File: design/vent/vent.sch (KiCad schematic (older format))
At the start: 20 parts, among them J1 Conn_01x02, J10 CS_TEST, J2 Conn_01x02, J3 SDA_TEST, J4 RX_TEST, J5 TX_TEST, J6 SCL_TEST, J7 SCK_TEST, J8 MISO_TEST, J9 MOSI_TEST

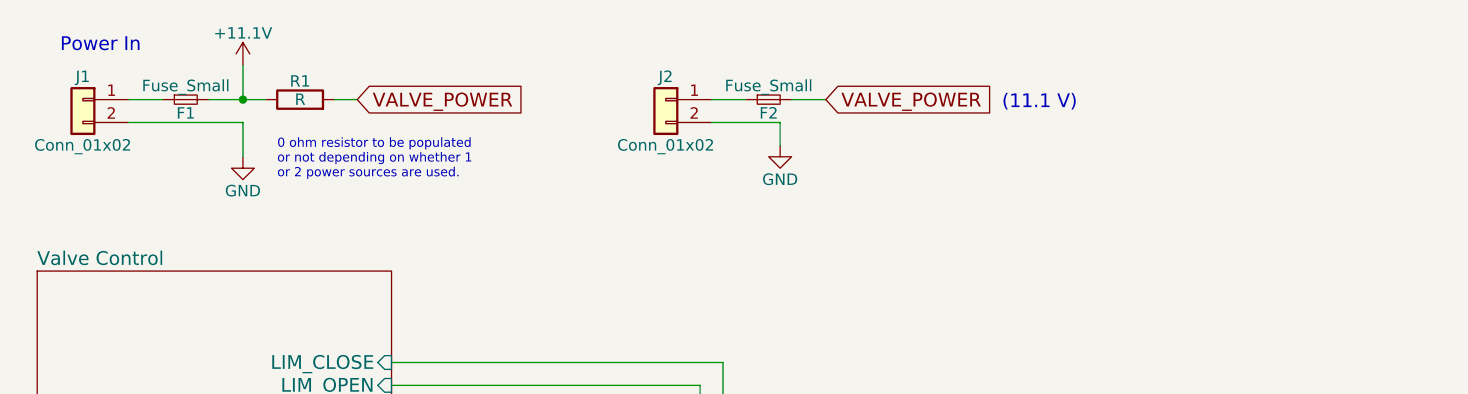
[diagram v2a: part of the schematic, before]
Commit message: Merge control power and analog sensor connectors
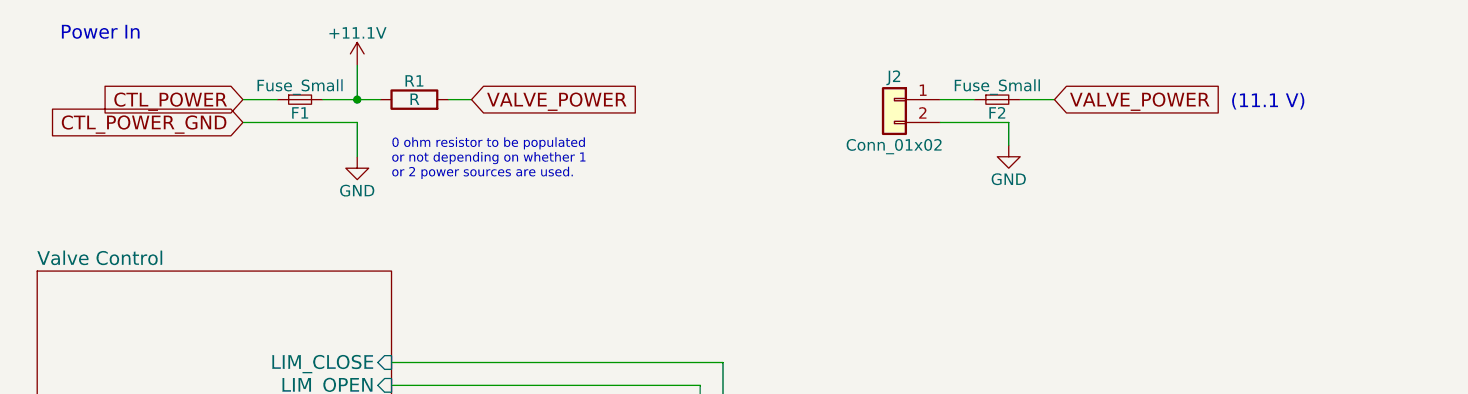
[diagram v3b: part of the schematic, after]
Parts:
- removed J1: Conn_01x02, symbol Conn_01x02
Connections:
- net CTL_POWER: now reaches F1.1
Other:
- moved on the sheet: F1, F2, J2, R1
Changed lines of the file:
@@
 NoConn ~ 6100 3650
 NoConn ~ 6100 3750
-$Comp
-L Conn_01x02 J1
-U 1 1 5ADF7D10
-P 1800 1350
-F 0 "J1" H 1800 1450 50  0000 C CNN
-F 1 "Conn_01x02" H 1800 1150 50  0000 C CNN
-F 2 "" H 1800 1350 50  0001 C CNN
-F 3 "" H 1800 1350 50  0001 C CNN
-	1    1800 1350
-	-1   0    0    -1
-$EndComp
-Text Notes 1700 1150 0    60   ~ 0
+Text Notes 1700 1100 0    60   ~ 0
 Power In
 $Comp
 L +11.1V #PWR1
 U 1 1 5ADF8011
-P 2500 1200
-F 0 "#PWR1" H 2500 1050 50  0001 C CNN
-F 1 "+11.1V" H 2500 1340 50  0000 C CNN
-F 2 "" H 2500 1200 50  0001 C CNN
-F 3 "" H 2500 1200 50  0001 C CNN
-	1    2500 1200
+P 3000 1200
+F 0 "#PWR1" H 3000 1050 50  0001 C CNN
+F 1 "+11.1V" H 3000 1340 50  0000 C CNN
+F 2 "" H 3000 1200 50  0001 C CNN
+F 3 "" H 3000 1200 50  0001 C CNN
+	1    3000 1200
 	1    0    0    -1
 $EndComp
@@
 L GND #PWR3
 U 1 1 5ADF8038
-P 2500 1600
-F 0 "#PWR3" H 2500 1350 50  0001 C CNN
-F 1 "GND" H 2500 1450 50  0000 C CNN
-F 2 "" H 2500 1600 50  0001 C CNN
-F 3 "" H 2500 1600 50  0001 C CNN
-	1    2500 1600
+P 3000 1600
+F 0 "#PWR3" H 3000 1350 50  0001 C CNN
+F 1 "GND" H 3000 1450 50  0000 C CNN
+F 2 "" H 3000 1600 50  0001 C CNN
+F 3 "" H 3000 1600 50  0001 C CNN
+	1    3000 1600
 	1    0    0    -1
 $EndComp
@@
 L Fuse_Small F1
 U 1 1 5AE9CD78
-P 2250 1350
-F 0 "F1" H 2250 1290 50  0000 C CNN
-F 1 "Fuse_Small" H 2250 1410 50  0000 C CNN
-F 2 "" H 2250 1350 50  0001 C CNN
-F 3 "" H 2250 1350 50  0001 C CNN
-	1    2250 1350
+P 2750 1350
+F 0 "F1" H 2750 1290 50  0000 C CNN
+F 1 "Fuse_Small" H 2750 1410 50  0000 C CNN
+F 2 "" H 2750 1350 50  0001 C CNN
+F 3 "" H 2750 1350 50  0001 C CNN
+	1    2750 1350
 	1    0    0    -1
 $EndComp
@@
 	4900 4950 5100 4950
 Wire Wire Line
-	2500 1200 2500 1350
-Wire Wire Line
-	2500 1450 2500 1600
-Wire Wire Line
-	2000 1450 2500 1450
+	3000 1200 3000 1350
+Wire Wire Line
+	3000 1450 3000 1600
+Wire Wire Line
+	2500 1450 3000 1450
 Wire Wire Line
 	5500 3250 5500 3050
@@
 Connection ~ 3900 5950
 Wire Wire Line
-	2000 1350 2150 1350
-Wire Wire Line
-	2350 1350 2600 1350
+	2500 1350 2650 1350
+Wire Wire Line
+	2850 1350 3100 1350
 Wire Wire Line
 	3150 2500 4600 2500
@@
 L Conn_01x02 J2
 U 1 1 5AEFA083
-P 4350 1350
-F 0 "J2" H 4350 1450 50  0000 C CNN
-F 1 "Conn_01x02" H 4350 1150 50  0000 C CNN
-F 2 "" H 4350 1350 50  0001 C CNN
-F 3 "" H 4350 1350 50  0001 C CNN
-	1    4350 1350
+P 5350 1350
+F 0 "J2" H 5350 1450 50  0000 C CNN
+F 1 "Conn_01x02" H 5350 1150 50  0000 C CNN
+F 2 "" H 5350 1350 50  0001 C CNN
+F 3 "" H 5350 1350 50  0001 C CNN
+	1    5350 1350
 	-1   0    0    -1
 $EndComp
@@
 L GND #PWR2
 U 1 1 5AEFA08B
-P 4850 1550
-F 0 "#PWR2" H 4850 1300 50  0001 C CNN
-F 1 "GND" H 4850 1400 50  0000 C CNN
-F 2 "" H 4850 1550 50  0001 C CNN
-F 3 "" H 4850 1550 50  0001 C CNN
-	1    4850 1550
+P 5850 1550
+F 0 "#PWR2" H 5850 1300 50  0001 C CNN
+F 1 "GND" H 5850 1400 50  0000 C CNN
+F 2 "" H 5850 1550 50  0001 C CNN
+F 3 "" H 5850 1550 50  0001 C CNN
+	1    5850 1550
 	-1   0    0    -1
 $EndComp
-Text Notes 6150 1400 2    60   ~ 0
+Text Notes 7150 1400 2    60   ~ 0
 (11.1 V)
 $Comp
 L Fuse_Small F2
 U 1 1 5AEFA092
-P 4800 1350
-F 0 "F2" H 4800 1290 50  0000 C CNN
-F 1 "Fuse_Small" H 4800 1410 50  0000 C CNN
-F 2 "" H 4800 1350 50  0001 C CNN
-F 3 "" H 4800 1350 50  0001 C CNN
-	1    4800 1350
-	1    0    0    -1
-$EndComp
-Wire Wire Line
-	4700 1350 4550 1350
-Wire Wire Line
-	4850 1550 4850 1450
-Wire Wire Line
-	4850 1450 4550 1450
-Wire Wire Line
-	5050 1350 4900 1350
-Text GLabel 5050 1350 2    60   Input ~ 0
+P 5800 1350
+F 0 "F2" H 5800 1290 50  0000 C CNN
+F 1 "Fuse_Small" H 5800 1410 50  0000 C CNN
+F 2 "" H 5800 1350 50  0001 C CNN
+F 3 "" H 5800 1350 50  0001 C CNN
+	1    5800 1350
+	1    0    0    -1
+$EndComp
+Wire Wire Line
+	5700 1350 5550 1350
+Wire Wire Line
+	5850 1550 5850 1450
+Wire Wire Line
+	5850 1450 5550 1450
+Wire Wire Line
+	6050 1350 5900 1350
+Text GLabel 6050 1350 2    60   Input ~ 0
 VALVE_POWER
-Text GLabel 3000 1350 2    60   Input ~ 0
+Text GLabel 3500 1350 2    60   Input ~ 0
 VALVE_POWER
 $Comp
 L R R1
 U 1 1 5AEFB0AE
-P 2750 1350
-F 0 "R1" V 2830 1350 50  0000 C CNN
-F 1 "R" V 2750 1350 50  0000 C CNN
-F 2 "" V 2680 1350 50  0001 C CNN
-F 3 "" H 2750 1350 50  0001 C CNN
-	1    2750 1350
+P 3250 1350
+F 0 "R1" V 3330 1350 50  0000 C CNN
+F 1 "R" V 3250 1350 50  0000 C CNN
+F 2 "" V 3180 1350 50  0001 C CNN
+F 3 "" H 3250 1350 50  0001 C CNN
+	1    3250 1350
 	0    -1   -1   0
 $EndComp
-Connection ~ 2500 1350
-Wire Wire Line
-	2900 1350 3000 1350
-Text Notes 2650 1700 0    40   ~ 0
+Connection ~ 3000 1350
+Wire Wire Line
+	3400 1350 3500 1350
+Text Notes 3150 1700 0    40   ~ 0
 0 ohm resistor to be populated\nor not depending on whether 1\nor 2 power sources are used.
+Text GLabel 2500 1350 0    60   Input ~ 0
+CTL_POWER
+Text GLabel 2500 1450 0    60   Input ~ 0
+CTL_POWER_GND
 $EndSCHEMATC

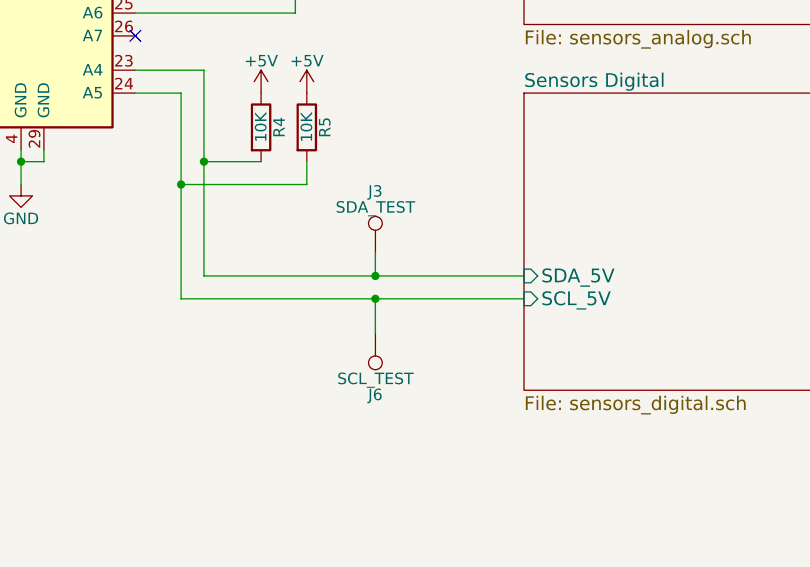
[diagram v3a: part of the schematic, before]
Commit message: Break out I2C lines on dsub connector
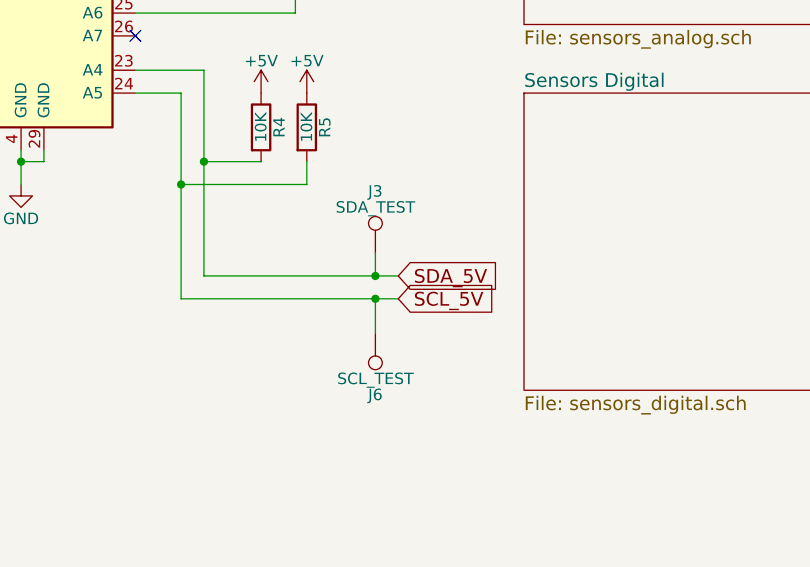
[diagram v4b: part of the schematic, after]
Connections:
- net Sensors Digital/SCL_5V renamed SCL_5V
- net Sensors Digital/SDA_5V renamed SDA_5V
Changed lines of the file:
@@
 F0 "Sensors Digital" 60
 F1 "sensors_digital.sch" 60
-F2 "SCL_5V" I L 7800 5900 60
-F3 "SDA_5V" I L 7800 5800 60
 $EndSheet
 $Sheet
@@
 	6400 4900 6400 5800
 Wire Wire Line
-	6400 5800 7800 5800
+	6400 5800 7250 5800
 Wire Wire Line
 	6650 5300 6400 5300
@@
 	7150 6050 7150 5900
 Wire Wire Line
-	7150 5700 7150 5800
-Connection ~ 7150 5800
+	7150 5800 7150 5700
 Wire Wire Line
 	6100 4250 6400 4250
@@
 	6300 5000 6300 5900
 Wire Wire Line
-	6300 5900 7800 5900
-Connection ~ 7150 5900
+	6300 5900 7250 5900
 Wire Wire Line
 	6100 4350 6500 4350
@@
 Text GLabel 2500 1450 0    60   Input ~ 0
 CTL_POWER_GND
+Text GLabel 7250 5800 2    60   Input ~ 0
+SDA_5V
+Text GLabel 7250 5900 2    60   Input ~ 0
+SCL_5V
+Connection ~ 7150 5800
+Connection ~ 7150 5900
 $EndSCHEMATC

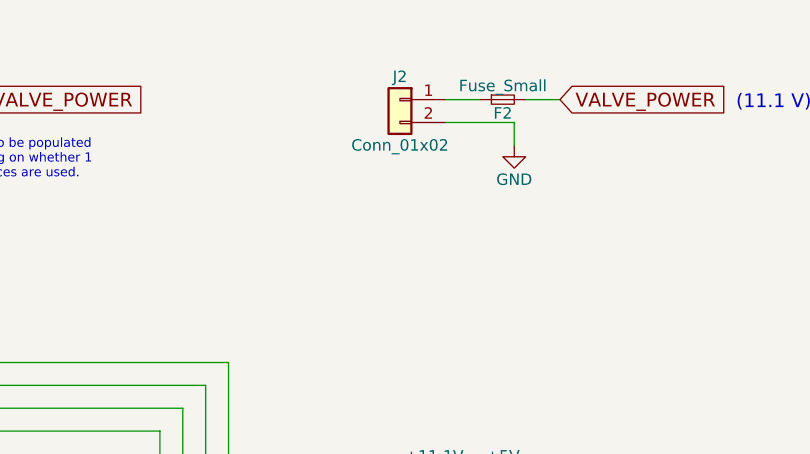
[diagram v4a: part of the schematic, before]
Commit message: Add connector part numbers to schematic
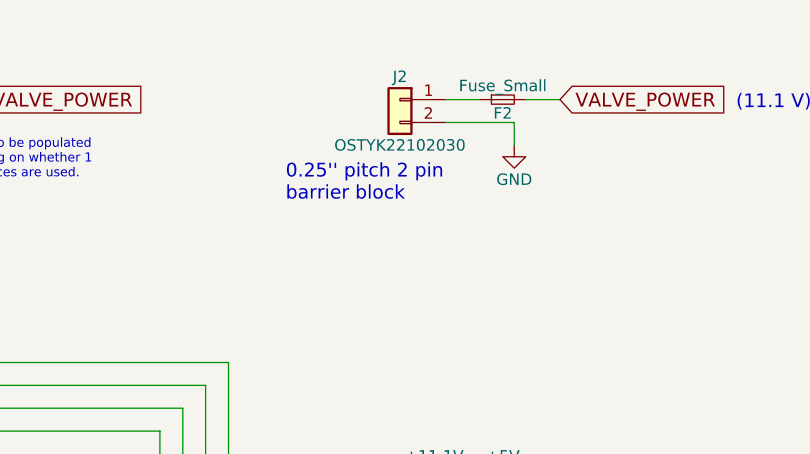
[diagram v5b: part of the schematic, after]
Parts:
- D1, D2: footprint (none) -> LEDs:LED_0805_HandSoldering
- J10, J3, J4, J5, J6, J7, J8, J9: footprint (none) -> TestPoint:TestPoint_Pad_D2.0mm
- J2: value Conn_01x02 -> OSTYK22102030
- R1, R2, R3, R4, R5: footprint (none) -> Resistors_SMD:R_0805_HandSoldering
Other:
- note added: "0.25'' pitch 2 pin\nbarrier block"
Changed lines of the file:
@@
 Power In
 $Comp
-L +11.1V #PWR1
+L +11.1V #PWR01
 U 1 1 5ADF8011
 P 3000 1200
-F 0 "#PWR1" H 3000 1050 50  0001 C CNN
+F 0 "#PWR01" H 3000 1050 50  0001 C CNN
 F 1 "+11.1V" H 3000 1340 50  0000 C CNN
 F 2 "" H 3000 1200 50  0001 C CNN
@@
 $EndComp
 $Comp
-L GND #PWR3
+L GND #PWR02
 U 1 1 5ADF8038
 P 3000 1600
-F 0 "#PWR3" H 3000 1350 50  0001 C CNN
+F 0 "#PWR02" H 3000 1350 50  0001 C CNN
 F 1 "GND" H 3000 1450 50  0000 C CNN
 F 2 "" H 3000 1600 50  0001 C CNN
@@
 $EndComp
 $Comp
-L +11.1V #PWR4
+L +11.1V #PWR03
 U 1 1 5ADF81C7
 P 5500 3050
-F 0 "#PWR4" H 5500 2900 50  0001 C CNN
+F 0 "#PWR03" H 5500 2900 50  0001 C CNN
 F 1 "+11.1V" H 5500 3190 50  0000 C CNN
 F 2 "" H 5500 3050 50  0001 C CNN
@@
 $EndComp
 $Comp
-L GND #PWR10
+L GND #PWR04
 U 1 1 5ADF8296
 P 5600 5400
-F 0 "#PWR10" H 5600 5150 50  0001 C CNN
+F 0 "#PWR04" H 5600 5150 50  0001 C CNN
 F 1 "GND" H 5600 5250 50  0000 C CNN
 F 2 "" H 5600 5400 50  0001 C CNN
@@
 $EndSheet
 $Comp
-L +5V #PWR5
+L +5V #PWR05
 U 1 1 5AE55261
 P 5800 3050
-F 0 "#PWR5" H 5800 2900 50  0001 C CNN
+F 0 "#PWR05" H 5800 2900 50  0001 C CNN
 F 1 "+5V" H 5800 3190 50  0000 C CNN
 F 2 "" H 5800 3050 50  0001 C CNN
@@
 F 0 "R4" V 6730 5150 50  0000 C CNN
 F 1 "10K" V 6650 5150 50  0000 C CNN
-F 2 "" V 6580 5150 50  0001 C CNN
+F 2 "Resistors_SMD:R_0805_HandSoldering" V 6580 5150 50  0001 C CNN
 F 3 "" H 6650 5150 50  0001 C CNN
 	1    6650 5150
@@
 $EndComp
 $Comp
-L +5V #PWR8
+L +5V #PWR06
 U 1 1 5AE848C6
 P 6650 5000
-F 0 "#PWR8" H 6650 4850 50  0001 C CNN
+F 0 "#PWR06" H 6650 4850 50  0001 C CNN
 F 1 "+5V" H 6650 5140 50  0000 C CNN
 F 2 "" H 6650 5000 50  0001 C CNN
@@
 F 0 "R5" V 6930 5150 50  0000 C CNN
 F 1 "10K" V 6850 5150 50  0000 C CNN
-F 2 "" V 6780 5150 50  0001 C CNN
+F 2 "Resistors_SMD:R_0805_HandSoldering" V 6780 5150 50  0001 C CNN
 F 3 "" H 6850 5150 50  0001 C CNN
 	1    6850 5150
@@
 $EndComp
 $Comp
-L +5V #PWR9
+L +5V #PWR07
 U 1 1 5AE84AB8
 P 6850 5000
-F 0 "#PWR9" H 6850 4850 50  0001 C CNN
+F 0 "#PWR07" H 6850 4850 50  0001 C CNN
 F 1 "+5V" H 6850 5140 50  0000 C CNN
 F 2 "" H 6850 5000 50  0001 C CNN
@@
 F 0 "J3" H 7150 5970 50  0000 C CNN
 F 1 "SDA_TEST" H 7150 5900 50  0000 C CNN
-F 2 "" H 7350 5700 50  0001 C CNN
+F 2 "TestPoint:TestPoint_Pad_D2.0mm" H 7350 5700 50  0001 C CNN
 F 3 "" H 7350 5700 50  0001 C CNN
 	1    7150 5700
@@
 F 0 "J6" H 7150 6320 50  0000 C CNN
 F 1 "SCL_TEST" H 7150 6250 50  0000 C CNN
-F 2 "" H 7350 6050 50  0001 C CNN
+F 2 "TestPoint:TestPoint_Pad_D2.0mm" H 7350 6050 50  0001 C CNN
 F 3 "" H 7350 6050 50  0001 C CNN
 	1    7150 6050
@@
 F 0 "J7" H 3850 7020 50  0000 C CNN
 F 1 "SCK_TEST" V 3950 6900 50  0000 C CNN
-F 2 "" H 4050 6750 50  0001 C CNN
+F 2 "TestPoint:TestPoint_Pad_D2.0mm" H 4050 6750 50  0001 C CNN
 F 3 "" H 4050 6750 50  0001 C CNN
 	1    3850 6750
@@
 F 0 "J8" H 4050 7020 50  0000 C CNN
 F 1 "MISO_TEST" V 4150 6900 50  0000 C CNN
-F 2 "" H 4250 6750 50  0001 C CNN
+F 2 "TestPoint:TestPoint_Pad_D2.0mm" H 4250 6750 50  0001 C CNN
 F 3 "" H 4250 6750 50  0001 C CNN
 	1    4050 6750
@@
 F 0 "J9" H 4250 7020 50  0000 C CNN
 F 1 "MOSI_TEST" V 4350 6900 50  0000 C CNN
-F 2 "" H 4450 6750 50  0001 C CNN
+F 2 "TestPoint:TestPoint_Pad_D2.0mm" H 4450 6750 50  0001 C CNN
 F 3 "" H 4450 6750 50  0001 C CNN
 	1    4250 6750
@@
 F 0 "J10" H 4450 7020 50  0000 C CNN
 F 1 "CS_TEST" V 4550 6900 50  0000 C CNN
-F 2 "" H 4650 6750 50  0001 C CNN
+F 2 "TestPoint:TestPoint_Pad_D2.0mm" H 4650 6750 50  0001 C CNN
 F 3 "" H 4650 6750 50  0001 C CNN
 	1    4450 6750
@@
 F 0 "J4" H 3700 6020 50  0000 C CNN
 F 1 "RX_TEST" V 3600 5900 50  0000 C CNN
-F 2 "" H 3900 5750 50  0001 C CNN
+F 2 "TestPoint:TestPoint_Pad_D2.0mm" H 3900 5750 50  0001 C CNN
 F 3 "" H 3900 5750 50  0001 C CNN
 	1    3700 5750
@@
 F 0 "J5" H 3900 6020 50  0000 C CNN
 F 1 "TX_TEST" V 3800 5900 50  0000 C CNN
-F 2 "" H 4100 5750 50  0001 C CNN
+F 2 "TestPoint:TestPoint_Pad_D2.0mm" H 4100 5750 50  0001 C CNN
 F 3 "" H 4100 5750 50  0001 C CNN
 	1    3900 5750
@@
 F 0 "D1" H 2600 4300 50  0000 C CNN
 F 1 "LED" H 2600 4100 50  0000 C CNN
-F 2 "" H 2600 4200 50  0001 C CNN
+F 2 "LEDs:LED_0805_HandSoldering" H 2600 4200 50  0001 C CNN
 F 3 "" H 2600 4200 50  0001 C CNN
 	1    2600 4200
@@
 F 0 "R2" V 2280 4200 50  0000 C CNN
 F 1 "100" V 2200 4200 50  0000 C CNN
-F 2 "" V 2130 4200 50  0001 C CNN
+F 2 "Resistors_SMD:R_0805_HandSoldering" V 2130 4200 50  0001 C CNN
 F 3 "" H 2200 4200 50  0001 C CNN
 	1    2200 4200
@@
 	2450 4200 2350 4200
 $Comp
-L GND #PWR6
+L GND #PWR08
 U 1 1 5AEE382E
 P 1900 4300
-F 0 "#PWR6" H 1900 4050 50  0001 C CNN
+F 0 "#PWR08" H 1900 4050 50  0001 C CNN
 F 1 "GND" H 1900 4150 50  0000 C CNN
 F 2 "" H 1900 4300 50  0001 C CNN
@@
 F 0 "D2" H 2600 4750 50  0000 C CNN
 F 1 "LED" H 2600 4550 50  0000 C CNN
-F 2 "" H 2600 4650 50  0001 C CNN
+F 2 "LEDs:LED_0805_HandSoldering" H 2600 4650 50  0001 C CNN
 F 3 "" H 2600 4650 50  0001 C CNN
 	1    2600 4650
@@
 F 0 "R3" V 2280 4650 50  0000 C CNN
 F 1 "100" V 2200 4650 50  0000 C CNN
-F 2 "" V 2130 4650 50  0001 C CNN
+F 2 "Resistors_SMD:R_0805_HandSoldering" V 2130 4650 50  0001 C CNN
 F 3 "" H 2200 4650 50  0001 C CNN
 	1    2200 4650
@@
 	2450 4650 2350 4650
 $Comp
-L GND #PWR7
+L GND #PWR09
 U 1 1 5AEE464D
 P 1900 4750
-F 0 "#PWR7" H 1900 4500 50  0001 C CNN
+F 0 "#PWR09" H 1900 4500 50  0001 C CNN
 F 1 "GND" H 1900 4600 50  0000 C CNN
 F 2 "" H 1900 4750 50  0001 C CNN
@@
 P 5350 1350
 F 0 "J2" H 5350 1450 50  0000 C CNN
-F 1 "Conn_01x02" H 5350 1150 50  0000 C CNN
+F 1 "OSTYK22102030" H 5350 1150 50  0000 C CNN
 F 2 "" H 5350 1350 50  0001 C CNN
 F 3 "" H 5350 1350 50  0001 C CNN
@@
 $EndComp
 $Comp
-L GND #PWR2
+L GND #PWR010
 U 1 1 5AEFA08B
 P 5850 1550
-F 0 "#PWR2" H 5850 1300 50  0001 C CNN
+F 0 "#PWR010" H 5850 1300 50  0001 C CNN
 F 1 "GND" H 5850 1400 50  0000 C CNN
 F 2 "" H 5850 1550 50  0001 C CNN
@@
 F 0 "R1" V 3330 1350 50  0000 C CNN
 F 1 "R" V 3250 1350 50  0000 C CNN
-F 2 "" V 3180 1350 50  0001 C CNN
+F 2 "Resistors_SMD:R_0805_HandSoldering" V 3180 1350 50  0001 C CNN
 F 3 "" H 3250 1350 50  0001 C CNN
 	1    3250 1350
@@
 Connection ~ 7150 5800
 Connection ~ 7150 5900
+Text Notes 4850 1800 0    60   ~ 0
+0.25'' pitch 2 pin\nbarrier block
 $EndSCHEMATC

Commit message: Add barrier block footprints
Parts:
- J2: footprint (none) -> Flight_Instr:Barrier_Strip_2Circuit
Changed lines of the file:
@@
 F 0 "J2" H 5350 1450 50  0000 C CNN
 F 1 "OSTYK22102030" H 5350 1150 50  0000 C CNN
-F 2 "" H 5350 1350 50  0001 C CNN
+F 2 "Flight_Instr:Barrier_Strip_2Circuit" H 5350 1350 50  0001 C CNN
 F 3 "" H 5350 1350 50  0001 C CNN
 	1    5350 1350

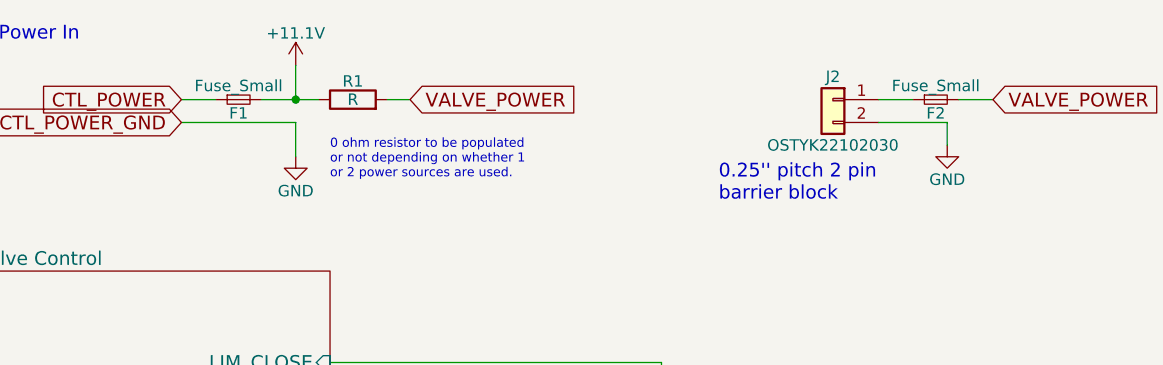
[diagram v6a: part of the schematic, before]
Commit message: Add more part numbers and footprints
- Flyback diodes
- Fuses
- Xbee
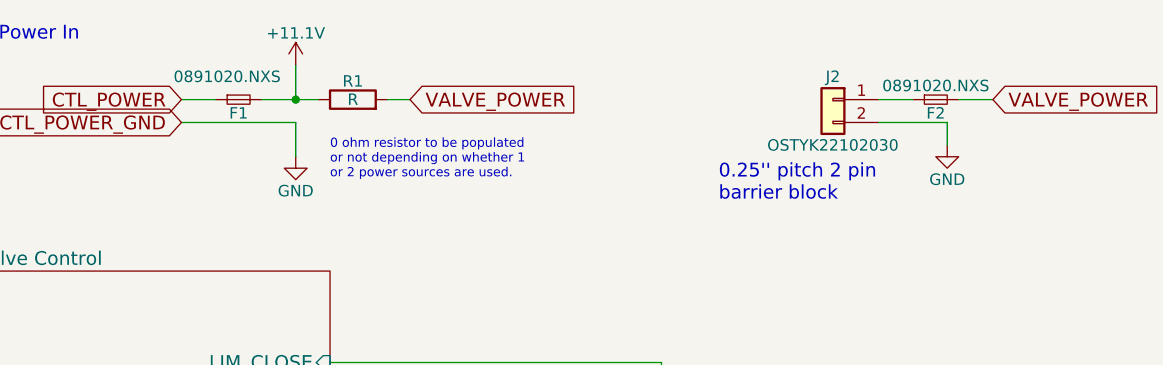
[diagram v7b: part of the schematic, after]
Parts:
- F1, F2: value Fuse_Small -> 0891020.NXS; footprint (none) -> Flight_Instr:PC_AutoFuse_Holder
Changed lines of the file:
@@
 P 2750 1350
 F 0 "F1" H 2750 1290 50  0000 C CNN
-F 1 "Fuse_Small" H 2750 1410 50  0000 C CNN
-F 2 "" H 2750 1350 50  0001 C CNN
+F 1 "0891020.NXS" H 2700 1450 50  0000 C CNN
+F 2 "Flight_Instr:PC_AutoFuse_Holder" H 2750 1350 50  0001 C CNN
 F 3 "" H 2750 1350 50  0001 C CNN
 	1    2750 1350
@@
 P 5800 1350
 F 0 "F2" H 5800 1290 50  0000 C CNN
-F 1 "Fuse_Small" H 5800 1410 50  0000 C CNN
-F 2 "" H 5800 1350 50  0001 C CNN
+F 1 "0891020.NXS" H 5800 1410 50  0000 C CNN
+F 2 "Flight_Instr:PC_AutoFuse_Holder" H 5800 1350 50  0001 C CNN
 F 3 "" H 5800 1350 50  0001 C CNN
 	1    5800 1350
